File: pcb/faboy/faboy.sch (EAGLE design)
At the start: 53 parts, among them U1 MAX1595UMAX, U2 MCP73831, Y1 16MHZ

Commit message: pcb > final with silk
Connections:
- removed net UVCC: C10.2, CN1.VBUS, F1.1, U$2.UVCC, U$2.VBUS
- new net VBUS: CN1.VBUS, F1.1
- net VIN: now also C10.2, U$2.UVCC, U$2.VBUS
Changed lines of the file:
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@@
-</segment>
-</net>
-<net name="UVCC" class="0">
-<segment>
-<pinref part="CN1" gate="G$1" pin="VBUS"/>
-<wire x1="33.02" y1="38.1" x2="38.1" y2="38.1" width="0.1524" layer="91"/>
-<wire x1="38.1" y1="38.1" x2="38.1" y2="43.18" width="0.1524" layer="91"/>
-<label x="38.1" y="45.72" size="1.778" layer="95"/>
-<pinref part="F1" gate="G$1" pin="1"/>
-<wire x1="38.1" y1="43.18" x2="38.1" y2="45.72" width="0.1524" layer="91"/>
-<wire x1="76.2" y1="40.64" x2="71.12" y2="40.64" width="0.1524" layer="91"/>
-<wire x1="71.12" y1="40.64" x2="71.12" y2="43.18" width="0.1524" layer="91"/>
-<wire x1="71.12" y1="43.18" x2="38.1" y2="43.18" width="0.1524" layer="91"/>
-<junction x="38.1" y="43.18"/>
-</segment>
-<segment>
-<pinref part="U$2" gate="G$1" pin="UVCC"/>
-<wire x1="73.66" y1="193.04" x2="71.12" y2="193.04" width="0.1524" layer="91"/>
-<wire x1="71.12" y1="193.04" x2="71.12" y2="205.74" width="0.1524" layer="91"/>
-<pinref part="U$2" gate="G$1" pin="VBUS"/>
-<wire x1="71.12" y1="205.74" x2="73.66" y2="205.74" width="0.1524" layer="91"/>
-<wire x1="71.12" y1="205.74" x2="71.12" y2="208.28" width="0.1524" layer="91"/>
-<junction x="71.12" y="205.74"/>
-<label x="68.58" y="208.28" size="1.778" layer="95"/>
-</segment>
-<segment>
-<pinref part="C10" gate="G$1" pin="2"/>
-<wire x1="15.24" y1="198.12" x2="15.24" y2="200.66" width="0.1524" layer="91"/>
-<label x="15.24" y="200.66" size="1.778" layer="95"/>
 </segment>
 </net>
@@
 <label x="266.7" y="45.72" size="1.778" layer="95"/>
 </segment>
+<segment>
+<pinref part="U$2" gate="G$1" pin="UVCC"/>
+<wire x1="73.66" y1="193.04" x2="71.12" y2="193.04" width="0.1524" layer="91"/>
+<wire x1="71.12" y1="193.04" x2="71.12" y2="205.74" width="0.1524" layer="91"/>
+<pinref part="U$2" gate="G$1" pin="VBUS"/>
+<wire x1="71.12" y1="205.74" x2="73.66" y2="205.74" width="0.1524" layer="91"/>
+<wire x1="71.12" y1="205.74" x2="71.12" y2="208.28" width="0.1524" layer="91"/>
+<junction x="71.12" y="205.74"/>
+<label x="68.58" y="208.28" size="1.778" layer="95"/>
+</segment>
+<segment>
+<pinref part="C10" gate="G$1" pin="2"/>
+<wire x1="15.24" y1="198.12" x2="15.24" y2="200.66" width="0.1524" layer="91"/>
+<label x="15.24" y="200.66" size="1.778" layer="95"/>
+</segment>
 </net>
 <net name="N$23" class="0">
@@
 </segment>
 </net>
+<net name="VBUS" class="0">
+<segment>
+<pinref part="F1" gate="G$1" pin="1"/>
+<wire x1="76.2" y1="40.64" x2="68.58" y2="40.64" width="0.1524" layer="91"/>
+<wire x1="68.58" y1="40.64" x2="68.58" y2="43.18" width="0.1524" layer="91"/>
+<wire x1="68.58" y1="43.18" x2="35.56" y2="43.18" width="0.1524" layer="91"/>
+<wire x1="35.56" y1="43.18" x2="35.56" y2="38.1" width="0.1524" layer="91"/>
+<pinref part="CN1" gate="G$1" pin="VBUS"/>
+<wire x1="35.56" y1="38.1" x2="33.02" y2="38.1" width="0.1524" layer="91"/>
+<label x="43.18" y="43.18" size="1.778" layer="95"/>
+</segment>
+</net>

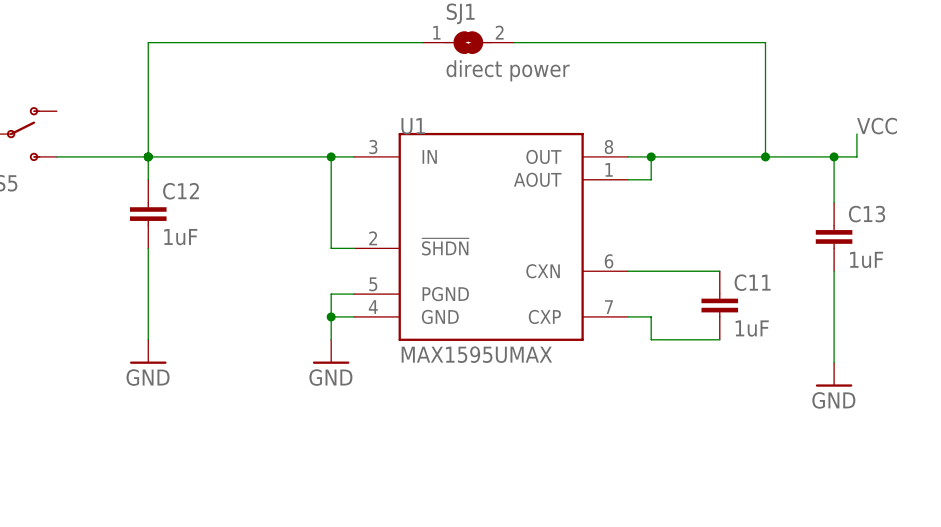
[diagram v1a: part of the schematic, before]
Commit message: soft > add faboy in core lib
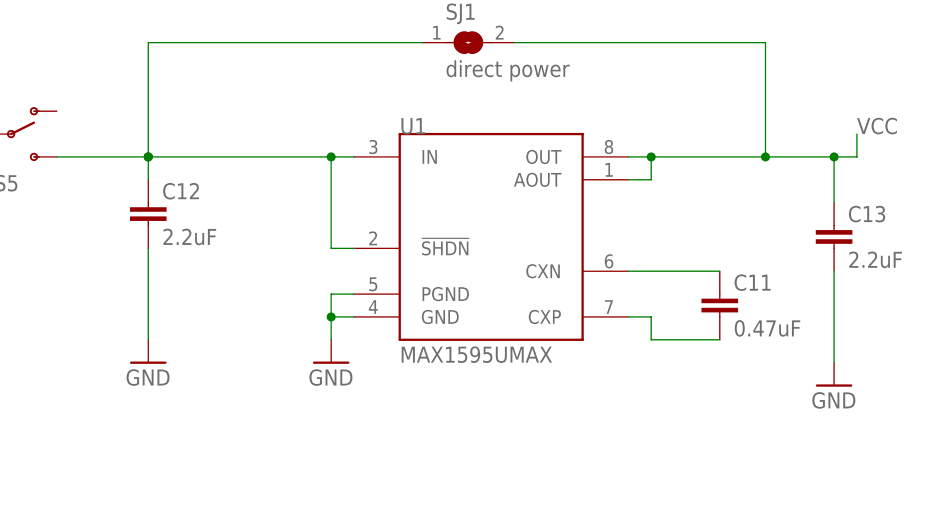
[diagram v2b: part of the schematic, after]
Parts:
- C11: value 1uF -> 0.47uF
- C12, C13: value 1uF -> 2.2uF
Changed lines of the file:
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@@
 <part name="GND14" library="supply1" deviceset="GND" device=""/>
 <part name="U1" library="maxim" deviceset="MAX1595" device="UMAX"/>
-<part name="C11" library="resistor" deviceset="C-EU" device="C0805K" value="1uF"/>
-<part name="C12" library="resistor" deviceset="C-EU" device="C0805K" value="1uF"/>
-<part name="C13" library="resistor" deviceset="C-EU" device="C0805K" value="1uF"/>
+<part name="C11" library="resistor" deviceset="C-EU" device="C0805K" value="0.47uF"/>
+<part name="C12" library="resistor" deviceset="C-EU" device="C0805K" value="2.2uF"/>
+<part name="C13" library="resistor" deviceset="C-EU" device="C0805K" value="2.2uF"/>
 <part name="GND15" library="supply1" deviceset="GND" device=""/>
 <part name="GND16" library="supply1" deviceset="GND" device=""/>
